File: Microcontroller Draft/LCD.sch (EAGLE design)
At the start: 2 parts

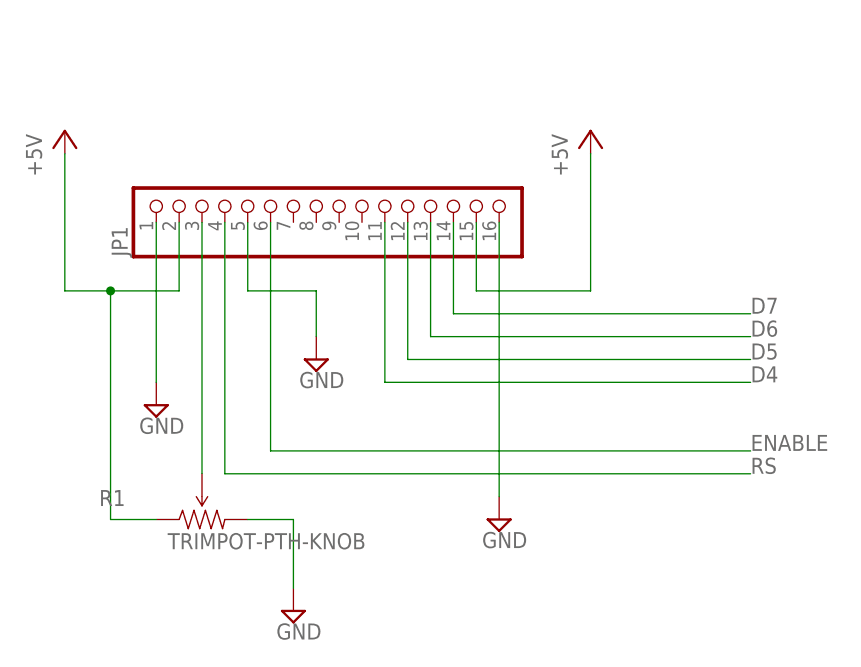
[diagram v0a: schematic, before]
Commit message: Used the awesome SparkFun LCD footprint
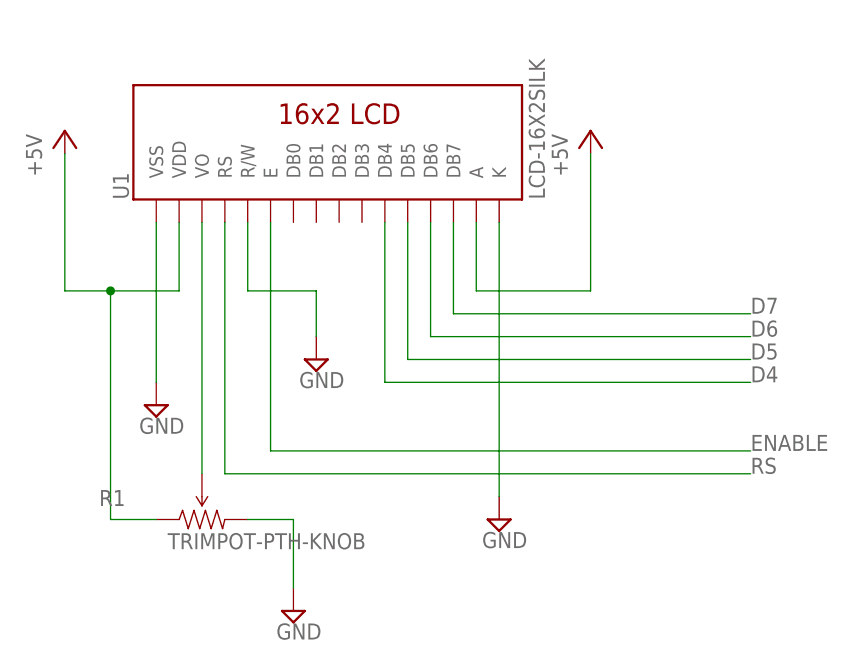
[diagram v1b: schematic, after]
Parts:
- removed JP1: (no value), pinhead:PINHD-1X16
- added U1: LCD-16X2SILK, SparkFun-Displays:LCD-16X2SILK
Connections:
- net +5V: now also U1.A, U1.VDD; no longer JP1.15, JP1.2
- net D4: now also U1.DB4; no longer JP1.11
- net D5: now also U1.DB5; no longer JP1.12
- net D6: now also U1.DB6; no longer JP1.13
- net D7: now also U1.DB7; no longer JP1.14
- net ENABLE: now also U1.E; no longer JP1.6
- net GND: now also U1.K, U1.R/W, U1.VSS; no longer JP1.1, JP1.16, JP1.5
- net N$3: now also U1.VO; no longer JP1.3
- net RS: now also U1.RS; no longer JP1.4
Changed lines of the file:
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@@
 </classes>
 <parts>
-<part name="JP1" library="pinhead" deviceset="PINHD-1X16" device=""/>
 <part name="R1" library="SparkFun-Electromechanical" deviceset="TRIMPOT" device="-PTH-KNOB"/>
 <part name="SUPPLY1" library="supply2" deviceset="GND" device=""/>
@@
 <part name="SUPPLY4" library="supply2" deviceset="GND" device=""/>
 <part name="P+2" library="supply1" deviceset="+5V" device=""/>
+<part name="U1" library="SparkFun-Displays" deviceset="LCD-16X2" device="SILK"/>
 </parts>
 <sheets>
@@
 </plain>
 <instances>
-<instance part="JP1" gate="A" x="78.74" y="96.52" rot="R90"/>
 <instance part="R1" gate="R?" x="66.04" y="60.96"/>
 <instance part="SUPPLY1" gate="GND" x="60.96" y="73.66"/>
@@
 <instance part="SUPPLY4" gate="GND" x="99.06" y="60.96"/>
 <instance part="P+2" gate="1" x="109.22" y="104.14"/>
+<instance part="U1" gate="G$1" x="81.28" y="104.14" rot="R90"/>
 </instances>
 <busses>
@@
 <net name="GND" class="0">
 <segment>
-<pinref part="JP1" gate="A" pin="1"/>
 <pinref part="SUPPLY1" gate="GND" pin="GND"/>
 <wire x1="60.96" y1="93.98" x2="60.96" y2="76.2" width="0.1524" layer="91"/>
+<pinref part="U1" gate="G$1" pin="VSS"/>
 </segment>
 <segment>
@@
 </segment>
 <segment>
-<pinref part="JP1" gate="A" pin="16"/>
 <wire x1="99.06" y1="93.98" x2="99.06" y2="63.5" width="0.1524" layer="91"/>
 <pinref part="SUPPLY4" gate="GND" pin="GND"/>
+<pinref part="U1" gate="G$1" pin="K"/>
 </segment>
 <segment>
-<pinref part="JP1" gate="A" pin="5"/>
 <wire x1="71.12" y1="93.98" x2="71.12" y2="86.36" width="0.1524" layer="91"/>
 <wire x1="71.12" y1="86.36" x2="78.74" y2="86.36" width="0.1524" layer="91"/>
 <pinref part="SUPPLY3" gate="GND" pin="GND"/>
 <wire x1="78.74" y1="86.36" x2="78.74" y2="81.28" width="0.1524" layer="91"/>
+<pinref part="U1" gate="G$1" pin="R/W"/>
 </segment>
 </net>
 <net name="+5V" class="0">
 <segment>
-<pinref part="JP1" gate="A" pin="2"/>
 <wire x1="63.5" y1="93.98" x2="63.5" y2="86.36" width="0.1524" layer="91"/>
 <pinref part="P+1" gate="1" pin="+5V"/>
@@
 <wire x1="55.88" y1="60.96" x2="55.88" y2="86.36" width="0.1524" layer="91"/>
 <junction x="55.88" y="86.36"/>
+<pinref part="U1" gate="G$1" pin="VDD"/>
 </segment>
 <segment>
-<pinref part="JP1" gate="A" pin="15"/>
 <wire x1="96.52" y1="93.98" x2="96.52" y2="86.36" width="0.1524" layer="91"/>
 <pinref part="P+2" gate="1" pin="+5V"/>
 <wire x1="96.52" y1="86.36" x2="109.22" y2="86.36" width="0.1524" layer="91"/>
 <wire x1="109.22" y1="86.36" x2="109.22" y2="101.6" width="0.1524" layer="91"/>
+<pinref part="U1" gate="G$1" pin="A"/>
 </segment>
 </net>
 <net name="N$3" class="0">
 <segment>
-<pinref part="JP1" gate="A" pin="3"/>
 <pinref part="R1" gate="R?" pin="WIPER"/>
 <wire x1="66.04" y1="93.98" x2="66.04" y2="66.04" width="0.1524" layer="91"/>
+<pinref part="U1" gate="G$1" pin="VO"/>
 </segment>
 </net>
 <net name="D7" class="0">
 <segment>
-<pinref part="JP1" gate="A" pin="14"/>
 <wire x1="93.98" y1="93.98" x2="93.98" y2="83.82" width="0.1524" layer="91"/>
 <wire x1="93.98" y1="83.82" x2="127" y2="83.82" width="0.1524" layer="91"/>
 <label x="127" y="83.82" size="1.778" layer="95"/>
+<pinref part="U1" gate="G$1" pin="DB7"/>
 </segment>
 </net>
 <net name="D6" class="0">
 <segment>
-<pinref part="JP1" gate="A" pin="13"/>
 <wire x1="91.44" y1="93.98" x2="91.44" y2="81.28" width="0.1524" layer="91"/>
 <wire x1="91.44" y1="81.28" x2="127" y2="81.28" width="0.1524" layer="91"/>
 <label x="127" y="81.28" size="1.778" layer="95"/>
+<pinref part="U1" gate="G$1" pin="DB6"/>
 </segment>
 </net>
 <net name="D5" class="0">
 <segment>
-<pinref part="JP1" gate="A" pin="12"/>
 <wire x1="88.9" y1="93.98" x2="88.9" y2="78.74" width="0.1524" layer="91"/>
 <wire x1="88.9" y1="78.74" x2="127" y2="78.74" width="0.1524" layer="91"/>
 <label x="127" y="78.74" size="1.778" layer="95"/>
+<pinref part="U1" gate="G$1" pin="DB5"/>
 </segment>
 </net>
 <net name="D4" class="0">
 <segment>
-<pinref part="JP1" gate="A" pin="11"/>
 <wire x1="86.36" y1="93.98" x2="86.36" y2="76.2" width="0.1524" layer="91"/>
 <wire x1="86.36" y1="76.2" x2="127" y2="76.2" width="0.1524" layer="91"/>
 <label x="127" y="76.2" size="1.778" layer="95"/>
+<pinref part="U1" gate="G$1" pin="DB4"/>
 </segment>
 </net>
 <net name="ENABLE" class="0">
 <segment>
-<pinref part="JP1" gate="A" pin="6"/>
 <wire x1="73.66" y1="93.98" x2="73.66" y2="68.58" width="0.1524" layer="91"/>
 <wire x1="73.66" y1="68.58" x2="127" y2="68.58" width="0.1524" layer="91"/>
 <label x="127" y="68.58" size="1.778" layer="95"/>
+<pinref part="U1" gate="G$1" pin="E"/>
 </segment>
 </net>
 <net name="RS" class="0">
 <segment>
-<pinref part="JP1" gate="A" pin="4"/>
 <wire x1="68.58" y1="93.98" x2="68.58" y2="66.04" width="0.1524" layer="91"/>
 <wire x1="68.58" y1="66.04" x2="127" y2="66.04" width="0.1524" layer="91"/>
 <label x="127" y="66.04" size="1.778" layer="95"/>
+<pinref part="U1" gate="G$1" pin="RS"/>
 </segment>
 </net>
